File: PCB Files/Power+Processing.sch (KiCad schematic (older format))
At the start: 12 parts

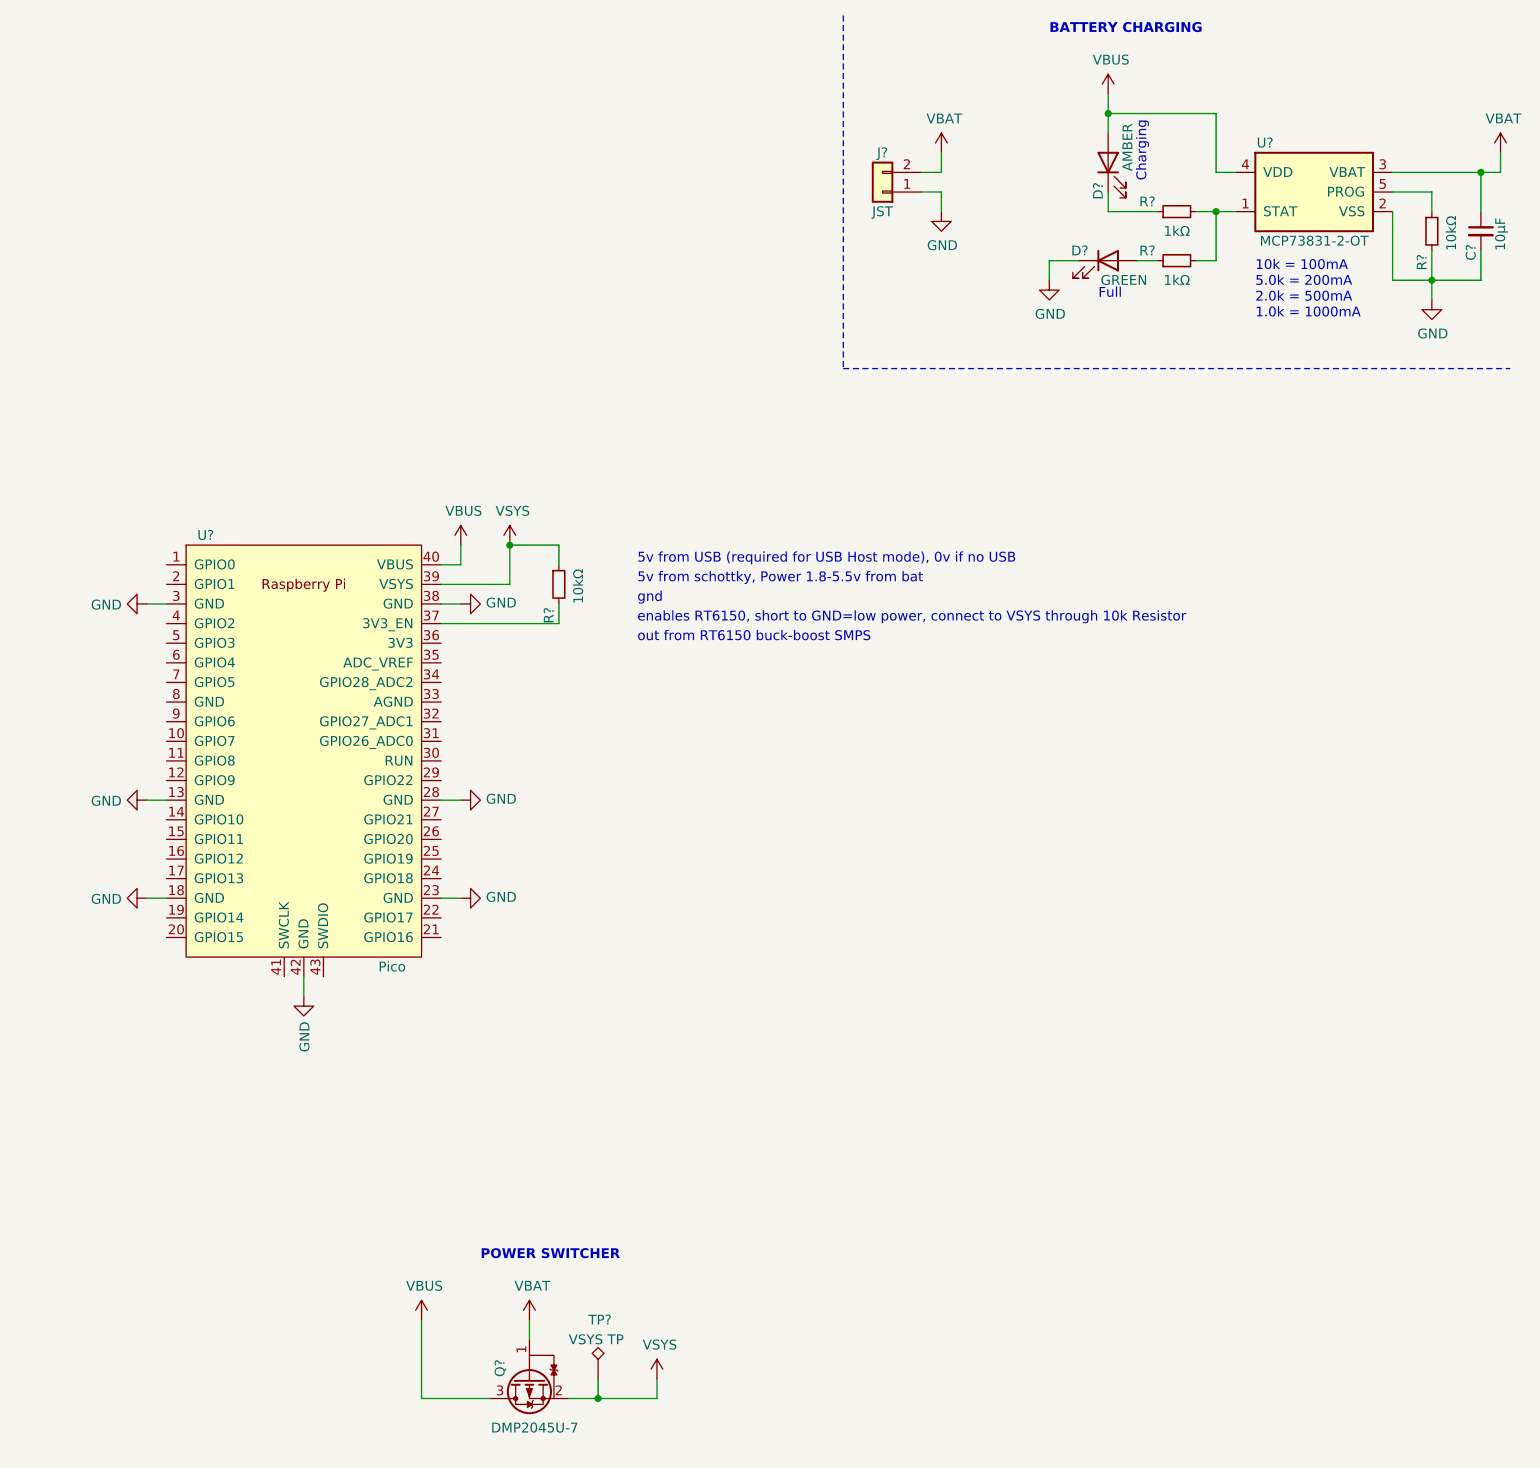
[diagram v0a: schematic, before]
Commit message: Added buttons, aux power distribution and connections to PI Pico
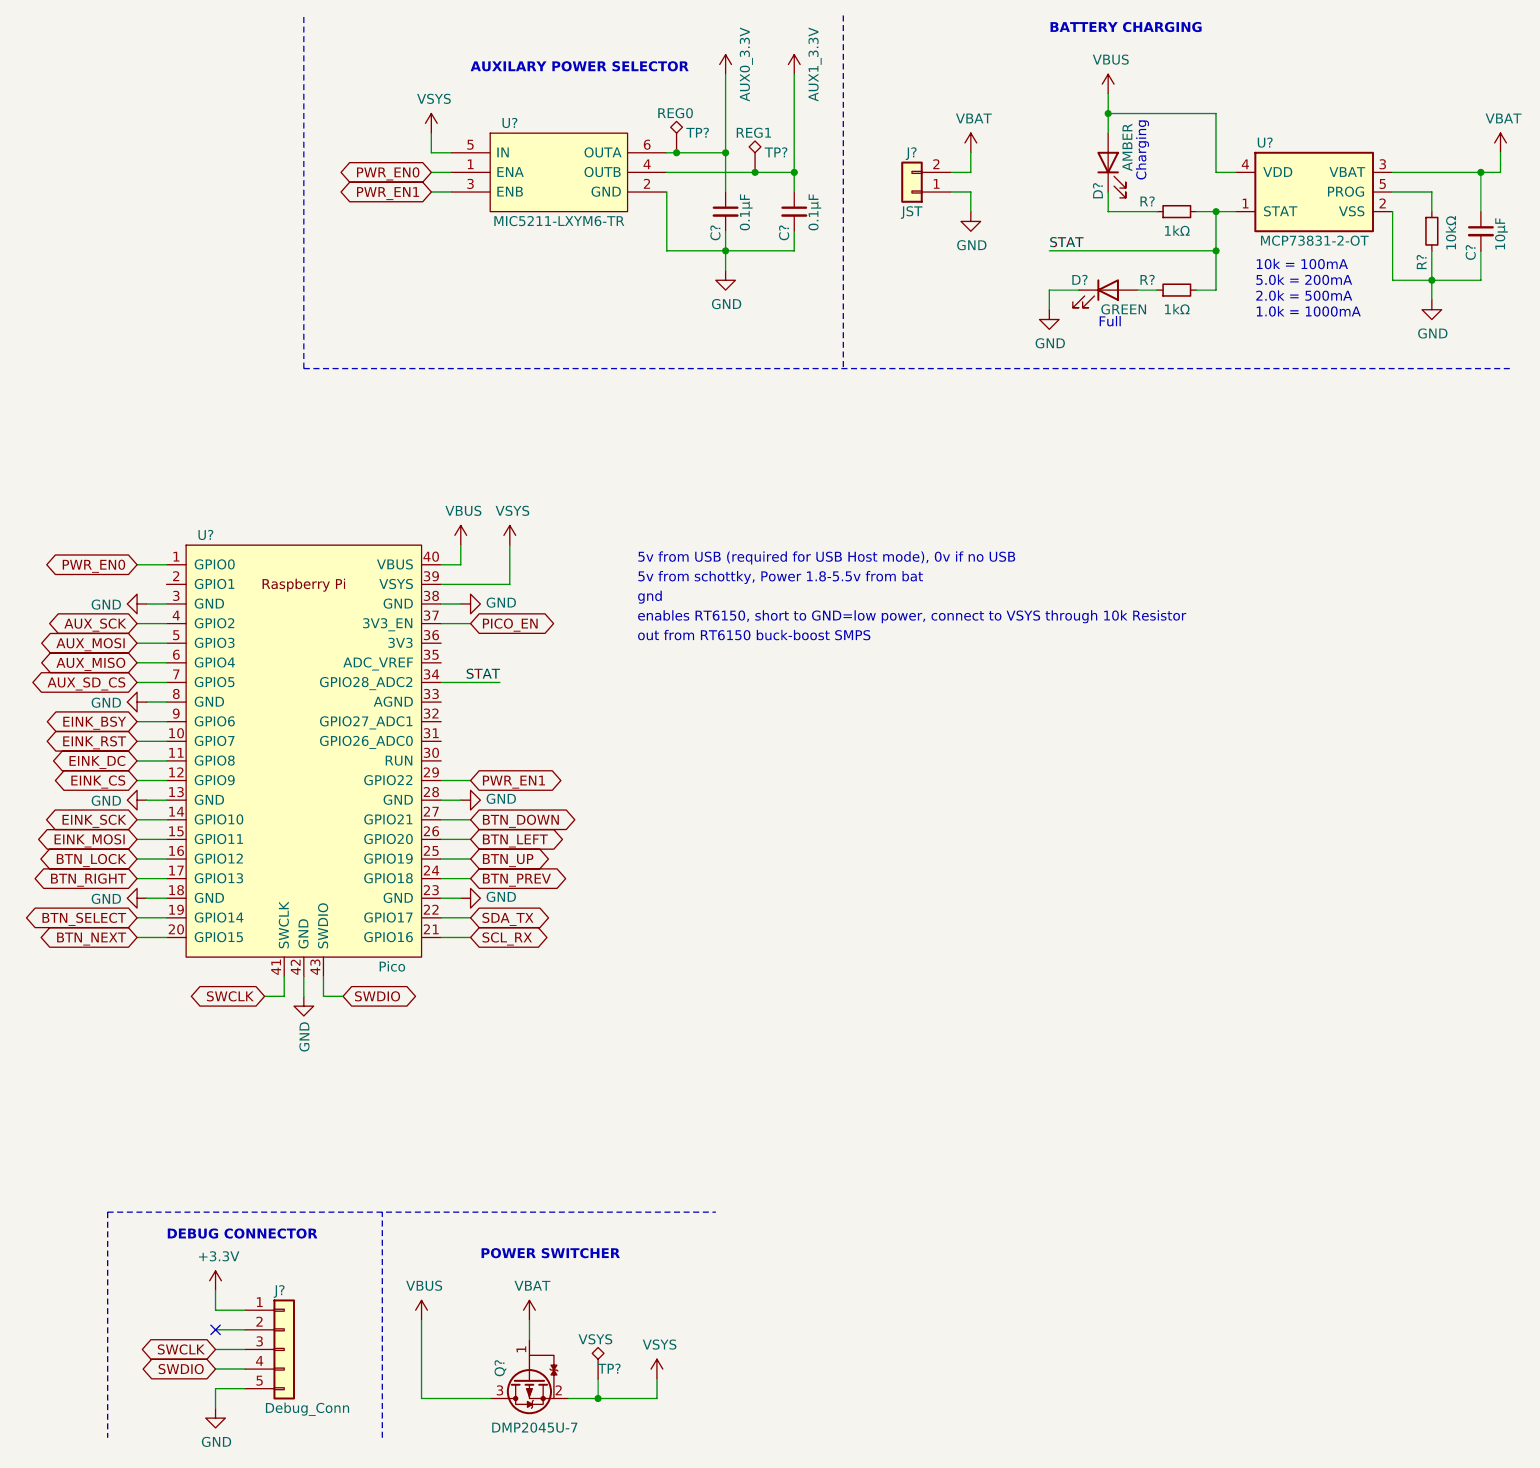
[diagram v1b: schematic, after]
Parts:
- removed R?: 10kΩ, symbol Device:R_Small
- added C? (x2): 0.1µF, symbol Device:C_Small
- added J?: Debug_Conn, symbol Connector_Generic:Conn_01x05
- added TP?: REG0, symbol Connector:TestPoint_Alt
- added TP?: REG1, symbol Connector:TestPoint_Alt
- added U?: MIC5211-LXYM6-TR, SOT95P280X100-6N, symbol E-ink-Pico:MIC5211-LXYM6-TR
- TP?: value VSYS TP -> VSYS
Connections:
- net GND: now also U?.8 (GND), C?.2, C?.2, J?.5 (Pin_5), U?.2 (GND)
- net VCC: now also C?.1, C?.1, TP?.1, TP?.1, U?.4 (OUTB), U?.5 (IN), U?.6 (OUTA)
- net PWR_EN0: now reaches U?.1 (GPIO0)
- net PWR_EN0: now also U?.1 (ENA)
- net EINK_RST: now reaches U?.10 (GPIO7)
- net EINK_DC: now reaches U?.11 (GPIO8)
- net EINK_CS: now reaches U?.12 (GPIO9)
- net EINK_SCK: now reaches U?.14 (GPIO10)
- net EINK_MOSI: now reaches U?.15 (GPIO11)
- net BTN_LOCK: now reaches U?.16 (GPIO12)
- net BTN_RIGHT: now reaches U?.17 (GPIO13)
- net BTN_SELECT: now reaches U?.19 (GPIO14)
- net BTN_NEXT: now reaches U?.20 (GPIO15)
- net SCL_RX: now reaches U?.21 (GPIO16)
- net SDA_TX: now reaches U?.22 (GPIO17)
- net BTN_PREV: now reaches U?.24 (GPIO18)
- net BTN_UP: now reaches U?.25 (GPIO19)
- net BTN_LEFT: now reaches U?.26 (GPIO20)
- net BTN_DOWN: now reaches U?.27 (GPIO21)
- net PWR_EN1: now reaches U?.29 (GPIO22)
- net PWR_EN1: now also U?.3 (ENB)
- net STAT: now reaches U?.34 (GPIO28_ADC2)
- net STAT: now also R?.2, R?.2, U?.1 (STAT)
- net PICO_EN: now reaches U?.37 (3V3_EN)
- net AUX_SCK: now reaches U?.4 (GPIO2)
- net SWCLK: now reaches U?.41 (SWCLK)
- net SWCLK: now also J?.3 (Pin_3)
- net SWDIO: now reaches U?.43 (SWDIO)
- net SWDIO: now also J?.4 (Pin_4)
- net AUX_MOSI: now reaches U?.5 (GPIO3)
- net AUX_MISO: now reaches U?.6 (GPIO4)
- net AUX_SD_CS: now reaches U?.7 (GPIO5)
- net EINK_BSY: now reaches U?.9 (GPIO6)
- new net +3V3: J?.1 (Pin_1)
- no-connect marks 0 -> 1
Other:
- note added: "AUXILARY POWER SELECTOR"
- note added: "DEBUG CONNECTOR"
- moved on the sheet: D?, J?, R?
